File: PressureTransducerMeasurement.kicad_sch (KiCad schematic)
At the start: 12 parts, among them J13 PT_1, J14 PT_4, J15 PT_2, J16 PT_5, J17 PT_3, J18 PT_6

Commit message: Actually fix PT3 and PT4 mapping
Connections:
- net PT_READING_3: now also J17.2 (Pin_2); no longer J14.2 (Pin_2)
- net PT_READING_4: now also J14.2 (Pin_2); no longer J17.2 (Pin_2)
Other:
- moved on the sheet: J14, J17
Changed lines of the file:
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@@
+	)
+	(junction
+		(at 185.42 77.47)
+		(diameter 0)
+		(color 0 0 0 0)
 	)
 	(junction
@@
 	)
 	(junction
+		(at 142.24 77.47)
+		(diameter 0)
+		(color 0 0 0 0)
+	)
+	(junction
 		(at 99.06 114.3)
 		(diameter 0)
 		(color 0 0 0 0)
 	)
-	(junction
-		(at 142.24 77.47)
-		(diameter 0)
-		(color 0 0 0 0)
-	)
-	(junction
-		(at 185.42 77.47)
-		(diameter 0)
-		(color 0 0 0 0)
-	)
 	(wire
 		(pts
@@
 	(wire
 		(pts
-			(xy 181.61 74.93) (xy 185.42 74.93)
-		)
-		(stroke
-			(width 0)
-			(type default)
-		)
-	)
-	(wire
-		(pts
 			(xy 102.87 74.93) (xy 95.25 74.93)
 		)
@@
 	(wire
 		(pts
+			(xy 102.87 111.76) (xy 95.25 111.76)
+		)
+		(stroke
+			(width 0)
+			(type default)
+		)
+	)
+	(wire
+		(pts
 			(xy 137.16 77.47) (xy 142.24 77.47)
 		)
@@
 	(wire
 		(pts
-			(xy 95.25 111.76) (xy 99.06 111.76)
+			(xy 102.87 114.3) (xy 99.06 114.3)
 		)
 		(stroke
@@
 	(wire
 		(pts
+			(xy 189.23 77.47) (xy 185.42 77.47)
+		)
+		(stroke
+			(width 0)
+			(type default)
+		)
+	)
+	(wire
+		(pts
 			(xy 143.51 120.65) (xy 143.51 124.46)
 		)
@@
 		(pts
 			(xy 142.24 77.47) (xy 142.24 78.74)
+		)
+		(stroke
+			(width 0)
+			(type default)
+		)
+	)
+	(wire
+		(pts
+			(xy 189.23 74.93) (xy 181.61 74.93)
 		)
 		(stroke
@@
 	(symbol
 		(lib_id "Connector_Generic:Conn_01x02")
-		(at 104.14 111.76 0)
+		(at 194.31 74.93 0)
 		(unit 1)
 		(exclude_from_sim no)
@@
 		(fields_autoplaced yes)
 		(property "Reference" "J17"
-			(at 106.68 111.7599 0)
+			(at 196.85 74.9299 0)
 			(effects
 				(font
@@
 		)
 		(property "Value" "PT_3"
-			(at 106.68 114.2999 0)
+			(at 196.85 77.4699 0)
 			(effects
 				(font
@@
 		)
 		(property "Footprint" "Connector_JST:JST_XH_B2B-XH-A_1x02_P2.50mm_Vertical"
-			(at 104.14 111.76 0)
+			(at 194.31 74.93 0)
 			(effects
 				(font
@@
 		)
 		(property "Datasheet" "~"
-			(at 104.14 111.76 0)
+			(at 194.31 74.93 0)
 			(effects
 				(font
@@
 		)
 		(property "Description" "Generic connector, single row, 01x02, script generated (kicad-library-utils/schlib/autogen/connector/)"
-			(at 104.14 111.76 0)
+			(at 194.31 74.93 0)
 			(effects
 				(font
@@
 		)
 		(property "MPN" "XH-2A"
-			(at 104.14 111.76 0)
+			(at 194.31 74.93 0)
 			(effects
 				(font
@@
 		)
 		(property "LCSC" "C20079"
-			(at 104.14 111.76 0)
+			(at 194.31 74.93 0)
 			(effects
 				(font
@@
 	(symbol
 		(lib_id "Connector_Generic:Conn_01x02")
-		(at 190.5 74.93 0)
+		(at 107.95 111.76 0)
 		(unit 1)
 		(exclude_from_sim no)
@@
 		(fields_autoplaced yes)
 		(property "Reference" "J14"
-			(at 193.04 74.9299 0)
+			(at 110.49 111.7599 0)
 			(effects
 				(font
@@
 		)
 		(property "Value" "PT_4"
-			(at 193.04 77.4699 0)
+			(at 110.49 114.2999 0)
 			(effects
 				(font
@@
 		)
 		(property "Footprint" "Connector_JST:JST_XH_B2B-XH-A_1x02_P2.50mm_Vertical"
-			(at 190.5 74.93 0)
+			(at 107.95 111.76 0)
 			(effects
 				(font
@@
 		)
 		(property "Datasheet" "~"
-			(at 190.5 74.93 0)
+			(at 107.95 111.76 0)
 			(effects
 				(font
@@
 		)
 		(property "Description" "Generic connector, single row, 01x02, script generated (kicad-library-utils/schlib/autogen/connector/)"
-			(at 190.5 74.93 0)
+			(at 107.95 111.76 0)
 			(effects
 				(font
@@
 		)
 		(property "MPN" "XH-2A"
-			(at 190.5 74.93 0)
+			(at 107.95 111.76 0)
 			(effects
 				(font
@@
 		)
 		(property "LCSC" "C20079"
-			(at 190.5 74.93 0)
-			(effects
-				(font
+			(at 107.95 111.76 0)
+			(effects
+				(font

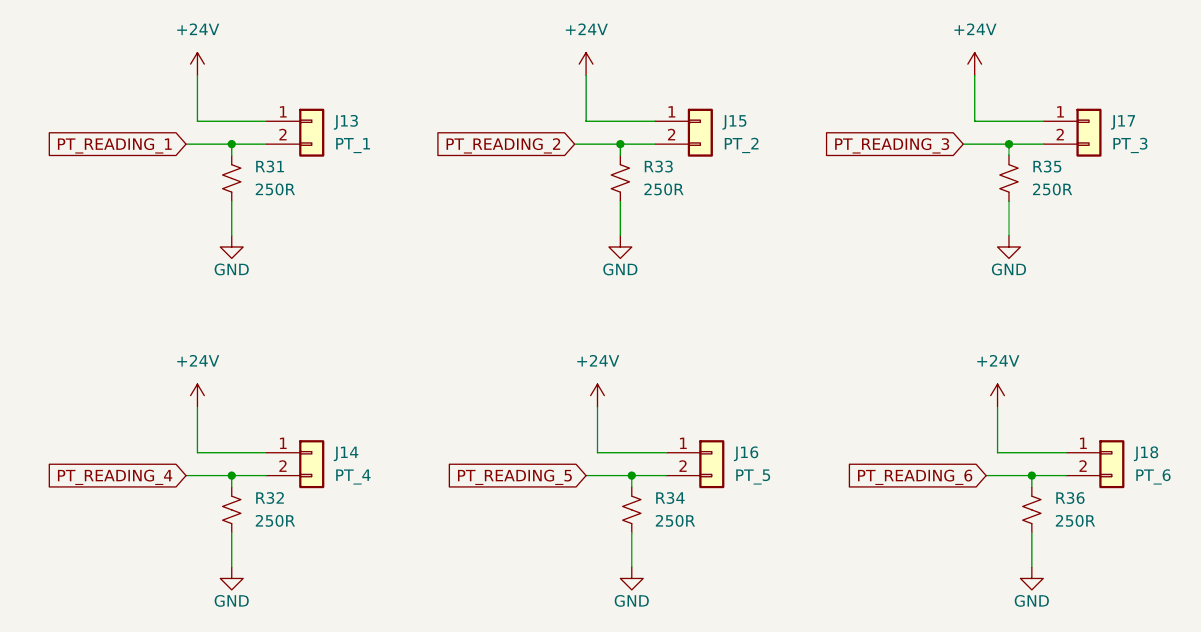
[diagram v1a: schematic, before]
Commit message: Swap PT3 and PT4 connectors so they are connected to teh proper pins
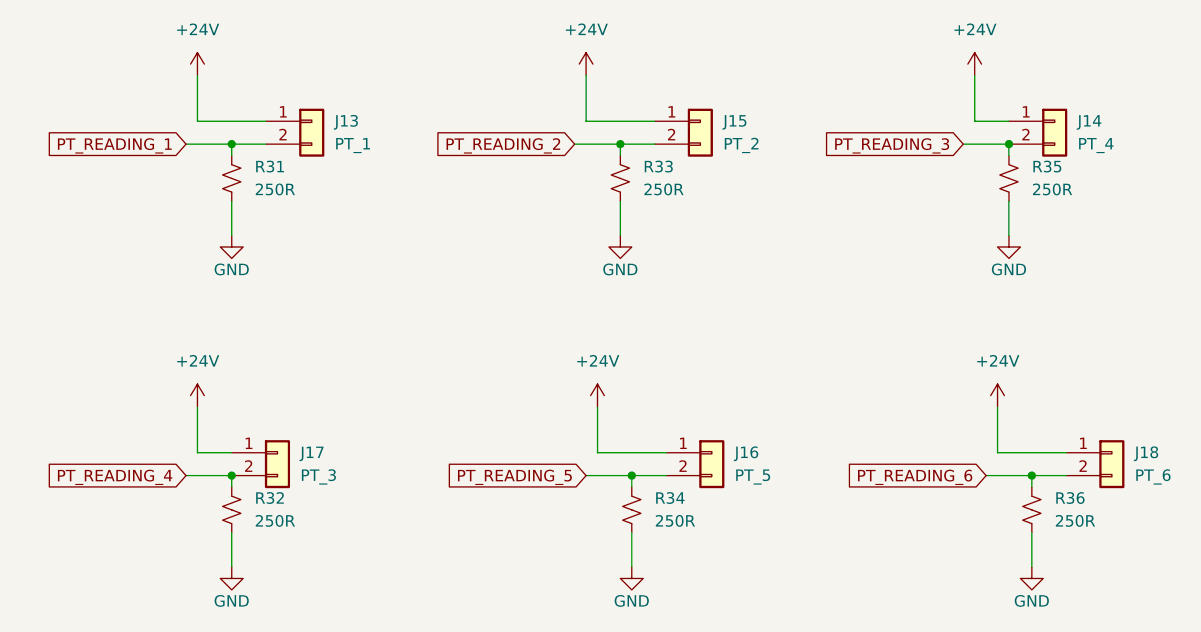
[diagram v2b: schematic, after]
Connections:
- net PT_READING_3: now also J14.2 (Pin_2); no longer J17.2 (Pin_2)
- net PT_READING_4: now also J17.2 (Pin_2); no longer J14.2 (Pin_2)
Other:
- moved on the sheet: J14, J17
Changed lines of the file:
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@@
+	)
+	(junction
+		(at 99.06 77.47)
+		(diameter 0)
+		(color 0 0 0 0)
+	)
+	(junction
+		(at 187.96 114.3)
+		(diameter 0)
+		(color 0 0 0 0)
+	)
+	(junction
+		(at 99.06 114.3)
+		(diameter 0)
+		(color 0 0 0 0)
+	)
+	(junction
+		(at 142.24 77.47)
+		(diameter 0)
+		(color 0 0 0 0)
 	)
 	(junction
@@
 		(color 0 0 0 0)
 	)
-	(junction
-		(at 99.06 77.47)
-		(diameter 0)
-		(color 0 0 0 0)
-	)
-	(junction
-		(at 187.96 114.3)
-		(diameter 0)
-		(color 0 0 0 0)
-	)
-	(junction
-		(at 142.24 77.47)
-		(diameter 0)
-		(color 0 0 0 0)
-	)
-	(junction
-		(at 99.06 114.3)
-		(diameter 0)
-		(color 0 0 0 0)
-	)
 	(wire
 		(pts
@@
 	(wire
 		(pts
+			(xy 181.61 74.93) (xy 185.42 74.93)
+		)
+		(stroke
+			(width 0)
+			(type default)
+		)
+	)
+	(wire
+		(pts
 			(xy 102.87 74.93) (xy 95.25 74.93)
 		)
@@
 	(wire
 		(pts
-			(xy 102.87 111.76) (xy 95.25 111.76)
-		)
-		(stroke
-			(width 0)
-			(type default)
-		)
-	)
-	(wire
-		(pts
 			(xy 137.16 77.47) (xy 142.24 77.47)
 		)
@@
 	(wire
 		(pts
-			(xy 102.87 114.3) (xy 99.06 114.3)
+			(xy 95.25 111.76) (xy 99.06 111.76)
 		)
 		(stroke
@@
 	(wire
 		(pts
-			(xy 189.23 77.47) (xy 185.42 77.47)
-		)
-		(stroke
-			(width 0)
-			(type default)
-		)
-	)
-	(wire
-		(pts
 			(xy 143.51 120.65) (xy 143.51 124.46)
 		)
@@
 		(pts
 			(xy 142.24 77.47) (xy 142.24 78.74)
-		)
-		(stroke
-			(width 0)
-			(type default)
-		)
-	)
-	(wire
-		(pts
-			(xy 189.23 74.93) (xy 181.61 74.93)
 		)
 		(stroke
@@
 	(symbol
 		(lib_id "Connector_Generic:Conn_01x02")
-		(at 194.31 74.93 0)
+		(at 104.14 111.76 0)
 		(unit 1)
 		(exclude_from_sim no)
@@
 		(fields_autoplaced yes)
 		(property "Reference" "J17"
-			(at 196.85 74.9299 0)
+			(at 106.68 111.7599 0)
 			(effects
 				(font
@@
 		)
 		(property "Value" "PT_3"
-			(at 196.85 77.4699 0)
+			(at 106.68 114.2999 0)
 			(effects
 				(font
@@
 		)
 		(property "Footprint" "Connector_JST:JST_XH_B2B-XH-A_1x02_P2.50mm_Vertical"
-			(at 194.31 74.93 0)
+			(at 104.14 111.76 0)
 			(effects
 				(font
@@
 		)
 		(property "Datasheet" "~"
-			(at 194.31 74.93 0)
+			(at 104.14 111.76 0)
 			(effects
 				(font
@@
 		)
 		(property "Description" "Generic connector, single row, 01x02, script generated (kicad-library-utils/schlib/autogen/connector/)"
-			(at 194.31 74.93 0)
+			(at 104.14 111.76 0)
 			(effects
 				(font
@@
 		)
 		(property "MPN" "XH-2A"
-			(at 194.31 74.93 0)
+			(at 104.14 111.76 0)
 			(effects
 				(font
@@
 		)
 		(property "LCSC" "C20079"
-			(at 194.31 74.93 0)
+			(at 104.14 111.76 0)
 			(effects
 				(font
@@
 	(symbol
 		(lib_id "Connector_Generic:Conn_01x02")
-		(at 107.95 111.76 0)
+		(at 190.5 74.93 0)
 		(unit 1)
 		(exclude_from_sim no)
@@
 		(fields_autoplaced yes)
 		(property "Reference" "J14"
-			(at 110.49 111.7599 0)
+			(at 193.04 74.9299 0)
 			(effects
 				(font
@@
 		)
 		(property "Value" "PT_4"
-			(at 110.49 114.2999 0)
+			(at 193.04 77.4699 0)
 			(effects
 				(font
@@
 		)
 		(property "Footprint" "Connector_JST:JST_XH_B2B-XH-A_1x02_P2.50mm_Vertical"
-			(at 107.95 111.76 0)
+			(at 190.5 74.93 0)
 			(effects
 				(font
@@
 		)
 		(property "Datasheet" "~"
-			(at 107.95 111.76 0)
+			(at 190.5 74.93 0)
 			(effects
 				(font
@@
 		)
 		(property "Description" "Generic connector, single row, 01x02, script generated (kicad-library-utils/schlib/autogen/connector/)"
-			(at 107.95 111.76 0)
+			(at 190.5 74.93 0)
 			(effects
 				(font
@@
 		)
 		(property "MPN" "XH-2A"
-			(at 107.95 111.76 0)
+			(at 190.5 74.93 0)
 			(effects
 				(font
@@
 		)
 		(property "LCSC" "C20079"
-			(at 107.95 111.76 0)
-			(effects
-				(font
+			(at 190.5 74.93 0)
+			(effects
+				(font
